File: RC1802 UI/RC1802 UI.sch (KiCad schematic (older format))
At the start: 44 parts, among them J1 Mount, J2 Mount, J3 Mount, J4 Mount, J6 CONN_02X20, SW1 CLEAR, SW10 IN5, SW11 IN6, SW12 IN7, SW2 IN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

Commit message: Fixed issue with in button, seems I should have read missing datasheet!
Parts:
- removed SW2: IN, switches:SPDT_PUSH, symbol SW_Push_SPDT
- added SW2: IN, switches:SPDT_PUSH, symbol NO/NC_Switch
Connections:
- net GND: now also SW2.3 (NC)
- net VCC: now also SW2.2 (NO)
- net at U1.3, U1.8: now also SW2.1 (C)
- no-connect marks 18 -> 17
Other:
- moved on the sheet: AFF1, AFF2, D1, D2, D3, D4, D5, D6, D7, J6, R1, R2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

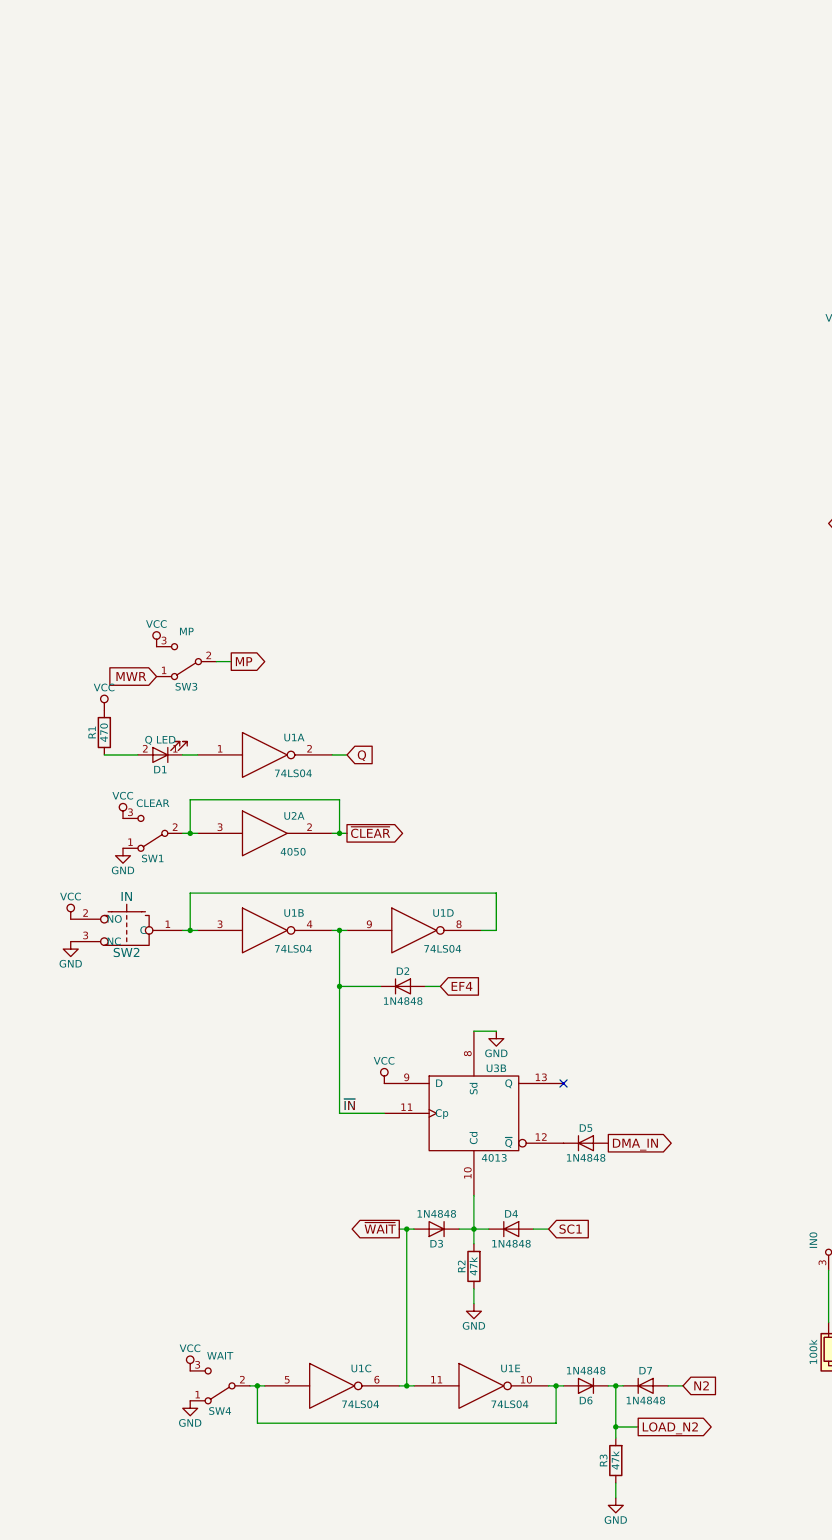
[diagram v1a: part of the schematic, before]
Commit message: Q signal inverter wrong way around!
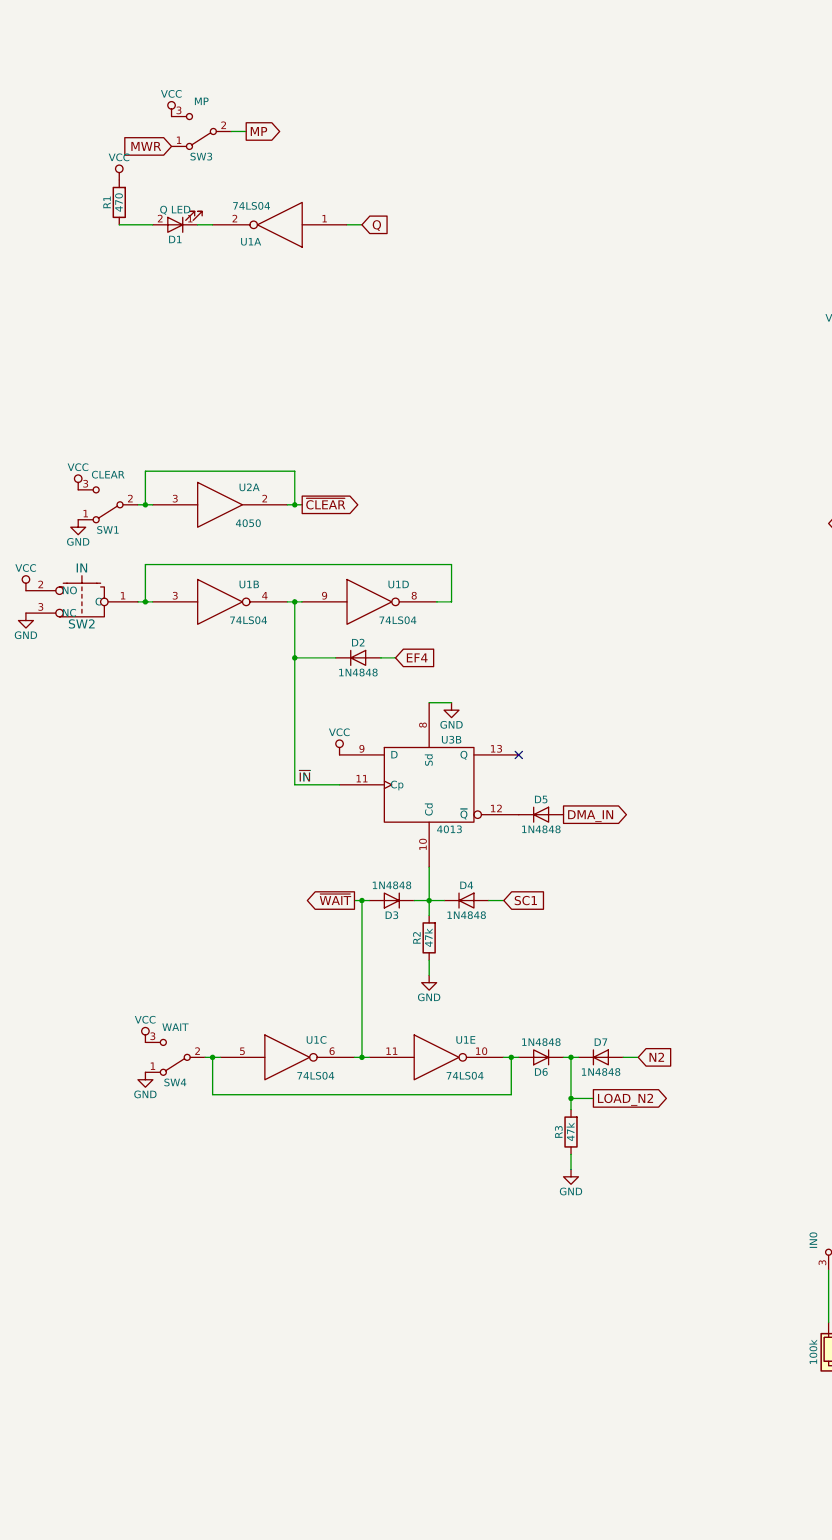
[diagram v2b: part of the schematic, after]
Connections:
- net Q: now also U1.1; no longer U1.2
- net at D1.1 (K): now also U1.2; no longer U1.1
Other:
- moved on the sheet: D1, D2, D3, D4, D5, D6, D7, R1, R2, R3, SW1, SW2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

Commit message: Bus connected in wrong order to hex drivers
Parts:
- AFF1: value MSB -> MSD
- AFF2: value LSB -> LSD
- U6: value 74LS245 -> 74LS244; symbol 74HC245 -> 74LS244
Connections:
- net BUS0: now also U7.5 (A); no longer U7.10 (D)
- net BUS1: now also U6.16 (O1a), U7.6 (B); no longer U6.17 (B1), U7.9 (C)
- net BUS2: now also U6.14 (O2a), U7.9 (C); no longer U6.16 (B2), U7.6 (B)
- net BUS3: now also U6.12 (O3a), U7.10 (D); no longer U6.15 (B3), U7.5 (A)
- net BUS4: now also U5.5 (A), U6.9 (O0b); no longer U5.10 (D), U6.14 (B4)
- net BUS5: now also U5.6 (B), U6.7 (O1b); no longer U5.9 (C), U6.13 (B5)
- net BUS6: now also U5.9 (C), U6.5 (O2b); no longer U5.6 (B), U6.12 (B6)
- net BUS7: now also U5.10 (D), U6.3 (O3b); no longer U5.5 (A), U6.11 (B7)
- net GND: no longer U2.7
- net LOAD_N2: now also U4.10; no longer U4.9
- net READ: now also U2.6, U6.1 (OEa); no longer U4.6
- net TPB: now also U4.11; no longer U4.10
- net VCC: no longer U6.1 (A->B)
- net at SW6.2 (B): now also U6.4 (I1a); no longer U6.3 (A1)
- net at SW7.2 (B): now also U6.6 (I2a); no longer U6.4 (A2)
- net at SW8.2 (B): now also U6.8 (I3a); no longer U6.5 (A3)
- net at SW9.2 (B): now also U6.11 (I0b); no longer U6.6 (A4)
- net at SW10.2 (B): now also U6.13 (I1b); no longer U6.7 (A5)
- net at SW11.2 (B): now also U6.15 (I2b); no longer U6.8 (A6)
- net at SW12.2 (B): now also U6.17 (I3b); no longer U6.9 (A7)
- net at U4.12: now also U4.9; no longer U4.11
- new net: U2.7, U4.6
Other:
- moved on the sheet: RN1, SW10, SW11, SW12, SW5, SW6, SW7, SW8, SW9, U2B, U2C, U4A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

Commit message: Removed resistor array as not in original schematic
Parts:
- removed RN1: 100k, Resistors_THT:R_Array_SIP9, symbol R_Network08
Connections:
- net VCC: now also SW10.3 (C), SW11.3 (C), SW12.3 (C), SW5.3 (C), SW6.3 (C), SW7.3 (C), SW8.3 (C), SW9.3 (C)
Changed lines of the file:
@@
 L VCC #PWR028
 U 1 1 595A4155
-P 6775 7700
-F 0 "#PWR028" H 6775 7550 50  0001 C CNN
-F 1 "VCC" H 6775 7850 50  0000 C CNN
-F 2 "" H 6775 7700 50  0001 C CNN
-F 3 "" H 6775 7700 50  0001 C CNN
-	1    6775 7700
-	0    1    1    0
+P 5775 7150
+F 0 "#PWR028" H 5775 7000 50  0001 C CNN
+F 1 "VCC" H 5775 7300 50  0000 C CNN
+F 2 "" H 5775 7150 50  0001 C CNN
+F 3 "" H 5775 7150 50  0001 C CNN
+	1    5775 7150
+	1    0    0    -1
 $EndComp
 $Comp
@@
 	14375 900  14375 950
 Connection ~ 14375 900
-$Comp
-L R_Network08 RN1
-U 1 1 594D0AD4
-P 6375 7500
-F 0 "RN1" V 5875 7500 50  0000 C CNN
-F 1 "100k" V 6775 7500 50  0000 C CNN
-F 2 "Resistors_THT:R_Array_SIP9" V 6850 7500 50  0001 C CNN
-F 3 "" H 6375 7500 50  0001 C CNN
-	1    6375 7500
-	-1   0    0    1
-$EndComp
 Wire Wire Line
 	6075 6950 6075 7300
@@
 	9675 7275 9675 6950
 Wire Wire Line
-	6775 7300 10275 7300
+	5775 7300 10275 7300
 Wire Wire Line
 	10275 7300 10275 6950
@@
 Wire Wire Line
 	6950 9475 7200 9475
+Connection ~ 6675 7300
+Connection ~ 6575 7300
+Connection ~ 6475 7300
+Connection ~ 6375 7300
+Connection ~ 6275 7300
+Connection ~ 6175 7300
+Connection ~ 6075 7300
+Wire Wire Line
+	5775 7150 5775 7300
 $EndSCHEMATC

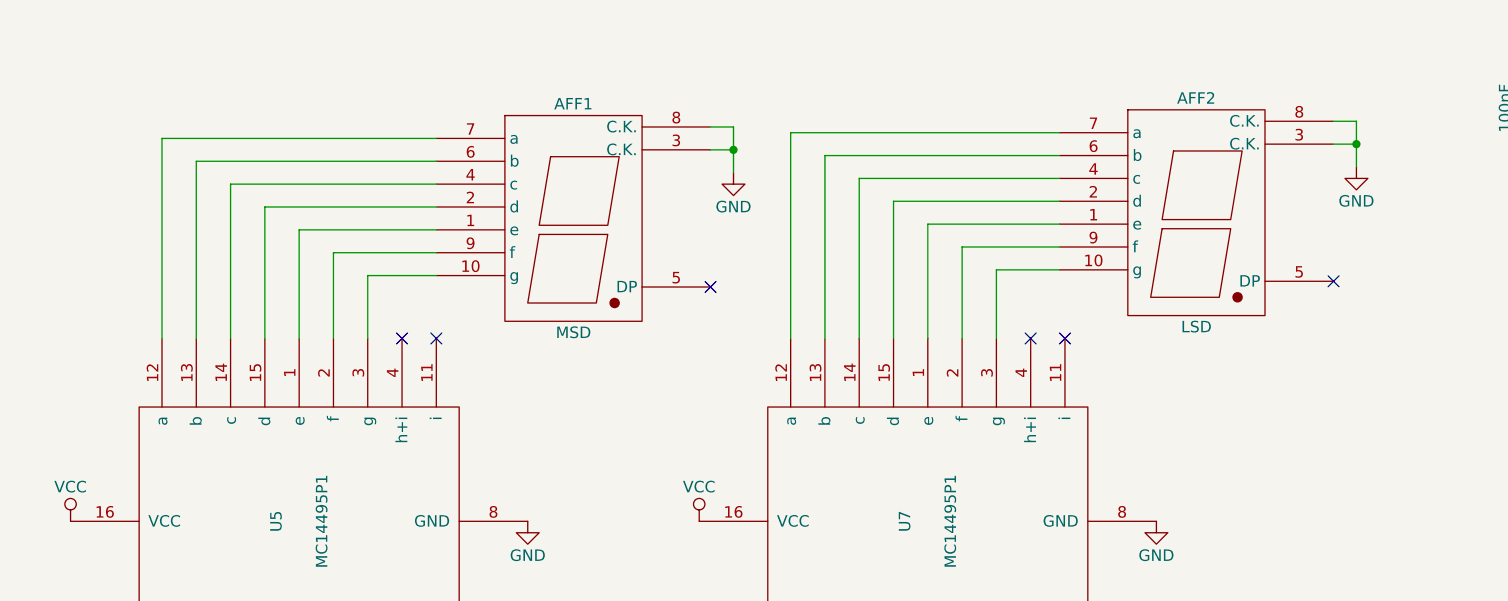
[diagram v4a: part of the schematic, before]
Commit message: Use LED digit DP as STROBE/READ indicator
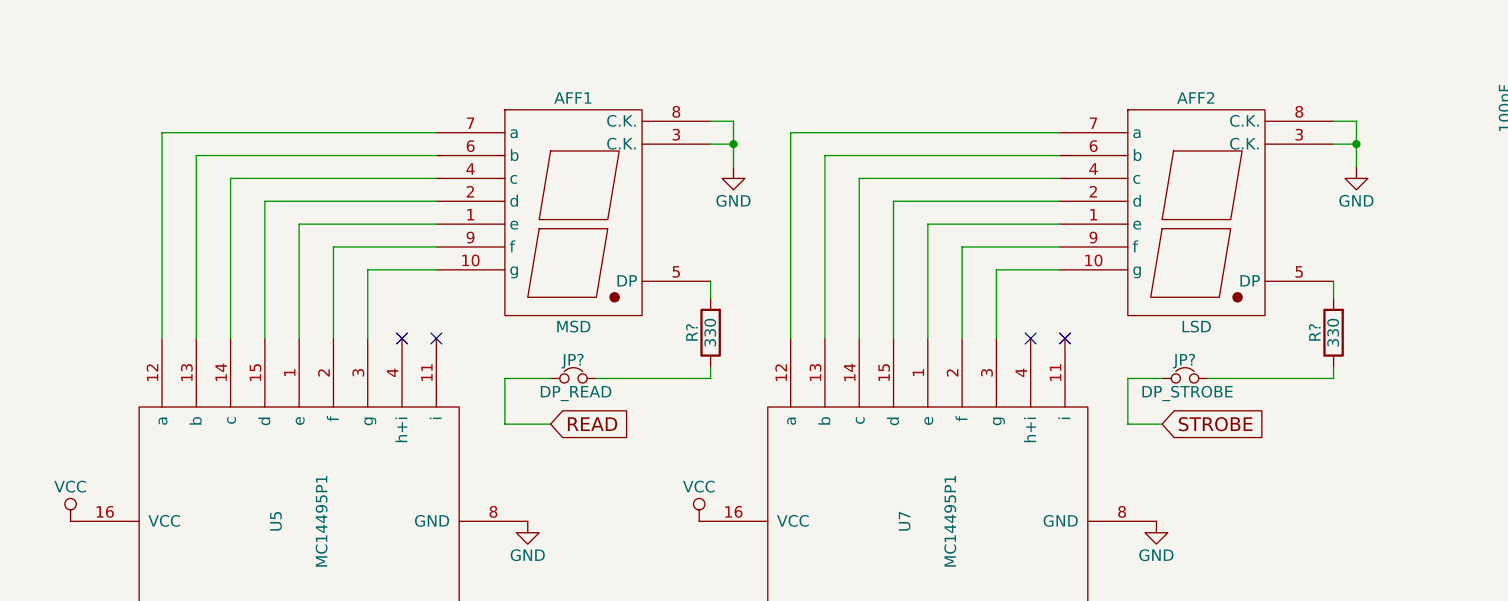
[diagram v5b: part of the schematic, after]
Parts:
- added JP?: DP_READ, symbol Jumper_NC_Small
- added JP?: DP_STROBE, symbol Jumper_NC_Small
- added R? (x2): 330, Resistors_THT:R_Axial_DIN0207_L6.3mm_D2.5mm_P10.16mm_Horizontal, symbol R
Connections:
- net READ: now also JP?.1
- net STROBE: now also JP?.1
- net at AFF1.5 (DP): now also R?.2
- net at AFF2.5 (DP): now also R?.2
- new net: JP?.2, R?.1 (x2)
- no-connect marks 17 -> 15
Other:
- moved on the sheet: AFF1
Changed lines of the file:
@@
 L LTS-6980HR AFF1
 U 1 1 594DB067
-P 8550 1575
-F 0 "AFF1" H 8550 2125 50  0000 C CNN
-F 1 "MSD" H 8550 1125 50  0000 C CNN
-F 2 "Displays_7-Segment:7SegmentLED_LTS6760_LTS6780" H 8550 1575 50  0001 C CNN
-F 3 "" H 8550 1575 50  0001 C CNN
-	1    8550 1575
+P 8550 1550
+F 0 "AFF1" H 8550 2100 50  0000 C CNN
+F 1 "MSD" H 8550 1100 50  0000 C CNN
+F 2 "Displays_7-Segment:7SegmentLED_LTS6760_LTS6780" H 8550 1550 50  0001 C CNN
+F 3 "" H 8550 1550 50  0001 C CNN
+	1    8550 1550
 	1    0    0    -1
 $EndComp
@@
 L GND #PWR026
 U 1 1 594DDA60
-P 9250 1325
-F 0 "#PWR026" H 9250 1075 50  0001 C CNN
-F 1 "GND" H 9250 1175 50  0000 C CNN
-F 2 "" H 9250 1325 50  0001 C CNN
-F 3 "" H 9250 1325 50  0001 C CNN
-	1    9250 1325
+P 9250 1300
+F 0 "#PWR026" H 9250 1050 50  0001 C CNN
+F 1 "GND" H 9250 1150 50  0000 C CNN
+F 2 "" H 9250 1300 50  0001 C CNN
+F 3 "" H 9250 1300 50  0001 C CNN
+	1    9250 1300
 	1    0    0    -1
 $EndComp
@@
 	1    0    0    -1
 $EndComp
-NoConn ~ 9150 1825
-NoConn ~ 11875 1800
 NoConn ~ 10550 2050
 NoConn ~ 10700 2050
@@
 	6850 3650 6850 3975
 Wire Wire Line
-	7950 1775 7650 1775
-Wire Wire Line
-	7650 1775 7650 2050
-Wire Wire Line
-	7950 1675 7500 1675
-Wire Wire Line
-	7500 1675 7500 2050
-Wire Wire Line
-	7950 1575 7350 1575
-Wire Wire Line
-	7350 1575 7350 2050
-Wire Wire Line
-	7200 2050 7200 1475
-Wire Wire Line
-	7200 1475 7950 1475
-Wire Wire Line
-	7950 1375 7050 1375
-Wire Wire Line
-	7050 1375 7050 2050
-Wire Wire Line
-	6900 2050 6900 1275
-Wire Wire Line
-	6900 1275 7950 1275
-Wire Wire Line
-	6750 2050 6750 1175
-Wire Wire Line
-	6750 1175 7950 1175
-Wire Wire Line
-	9150 1225 9250 1225
-Wire Wire Line
-	9250 1125 9250 1325
-Wire Wire Line
-	9250 1125 9150 1125
-Connection ~ 9250 1225
+	7950 1750 7650 1750
+Wire Wire Line
+	7650 1750 7650 2050
+Wire Wire Line
+	7950 1650 7500 1650
+Wire Wire Line
+	7500 1650 7500 2050
+Wire Wire Line
+	7950 1550 7350 1550
+Wire Wire Line
+	7350 1550 7350 2050
+Wire Wire Line
+	7200 1450 7200 2050
+Wire Wire Line
+	7200 1450 7950 1450
+Wire Wire Line
+	7950 1350 7050 1350
+Wire Wire Line
+	7050 1350 7050 2050
+Wire Wire Line
+	6900 1250 6900 2050
+Wire Wire Line
+	6900 1250 7950 1250
+Wire Wire Line
+	6750 1150 6750 2050
+Wire Wire Line
+	6750 1150 7950 1150
+Wire Wire Line
+	9150 1200 9250 1200
+Wire Wire Line
+	9250 1100 9250 1300
+Wire Wire Line
+	9250 1100 9150 1100
+Connection ~ 9250 1200
 Wire Wire Line
 	11875 1200 11975 1200
@@
 Wire Wire Line
 	5775 7150 5775 7300
+$Comp
+L Jumper_NC_Small JP?
+U 1 1 5B990FBF
+P 8550 2225
+F 0 "JP?" H 8550 2305 50  0000 C CNN
+F 1 "DP_READ" H 8560 2165 50  0000 C CNN
+F 2 "" H 8550 2225 50  0001 C CNN
+F 3 "" H 8550 2225 50  0001 C CNN
+	1    8550 2225
+	1    0    0    -1
+$EndComp
+Wire Wire Line
+	8650 2225 9150 2225
+$Comp
+L Jumper_NC_Small JP?
+U 1 1 5B99266E
+P 11225 2225
+F 0 "JP?" H 11225 2305 50  0000 C CNN
+F 1 "DP_STROBE" H 11235 2165 50  0000 C CNN
+F 2 "" H 11225 2225 50  0001 C CNN
+F 3 "" H 11225 2225 50  0001 C CNN
+	1    11225 2225
+	1    0    0    -1
+$EndComp
+Wire Wire Line
+	11875 2225 11325 2225
+Text GLabel 11125 2425 2    60   Input ~ 0
+STROBE
+Wire Wire Line
+	11125 2425 10975 2425
+Wire Wire Line
+	10975 2425 10975 2225
+Wire Wire Line
+	10975 2225 11125 2225
+Text GLabel 8450 2425 2    60   Input ~ 0
+READ
+Wire Wire Line
+	8450 2425 8250 2425
+Wire Wire Line
+	8250 2425 8250 2225
+Wire Wire Line
+	8250 2225 8450 2225
+$Comp
+L R R?
+U 1 1 5B995582
+P 11875 2025
+F 0 "R?" V 11955 2025 50  0000 C CNN
+F 1 "330" V 11875 2025 50  0000 C CNN
+F 2 "Resistors_THT:R_Axial_DIN0207_L6.3mm_D2.5mm_P10.16mm_Horizontal" V 11805 2025 50  0001 C CNN
+F 3 "" H 11875 2025 50  0001 C CNN
+	1    11875 2025
+	-1   0    0    1
+$EndComp
+Wire Wire Line
+	11875 2175 11875 2225
+Wire Wire Line
+	11875 1875 11875 1800
+$Comp
+L R R?
+U 1 1 5B995F7C
+P 9150 2025
+F 0 "R?" V 9230 2025 50  0000 C CNN
+F 1 "330" V 9150 2025 50  0000 C CNN
+F 2 "Resistors_THT:R_Axial_DIN0207_L6.3mm_D2.5mm_P10.16mm_Horizontal" V 9080 2025 50  0001 C CNN
+F 3 "" H 9150 2025 50  0001 C CNN
+	1    9150 2025
+	-1   0    0    1
+$EndComp
+Wire Wire Line
+	9150 1800 9150 1875
+Wire Wire Line
+	9150 2225 9150 2175
 $EndSCHEMATC

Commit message: Added ~Q to UI connector
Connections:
- net GND: now also U1.1; no longer J6.26 (P26)
- net Q: no longer U1.1
- net at U1.2: no longer D1.1 (K)
- new net ~Q: D1.1 (K), J6.26 (P26)
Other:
- moved on the sheet: D1, J6, R1, U1A

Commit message: Regenerate netlist
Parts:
- JP1, JP2: renamed from JP?; footprint (none) -> Pin_Headers:Pin_Header_Straight_1x02_Pitch2.54mm
- gave numbers to parts that had none: 2
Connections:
- net Q: no longer names the net of J6.25 (P25)
- no-connect marks 15 -> 16
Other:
- moved on the sheet: AFF1, AFF2, JP1, JP2, R4, R5, U5, U7

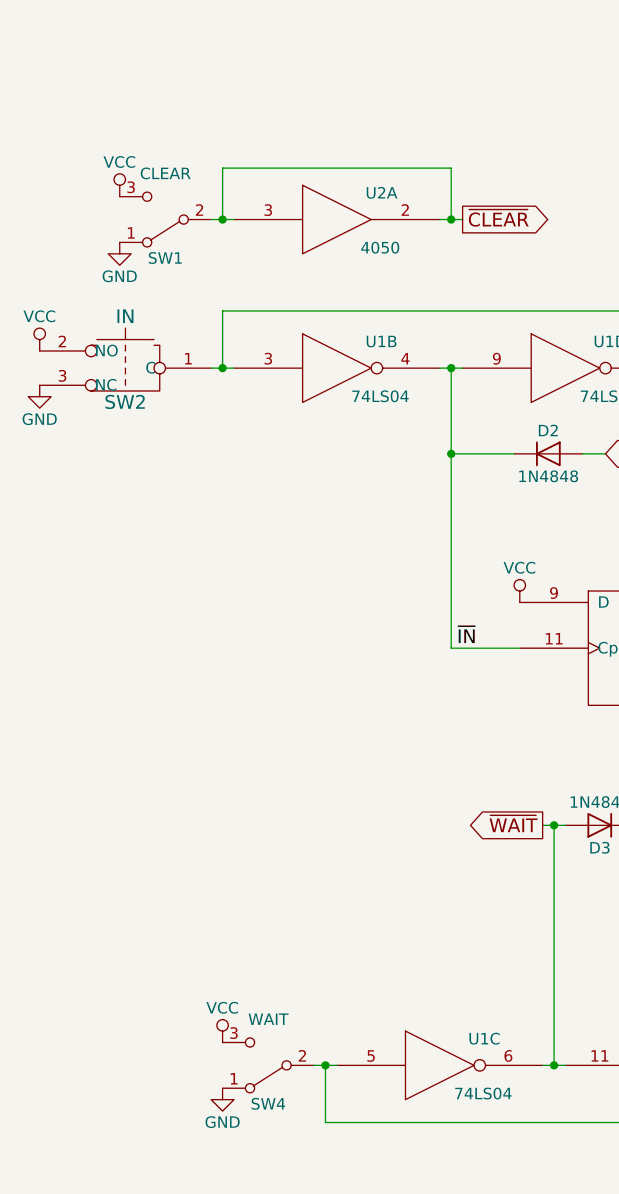
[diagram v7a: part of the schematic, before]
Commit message: Use proper switch names to ease use
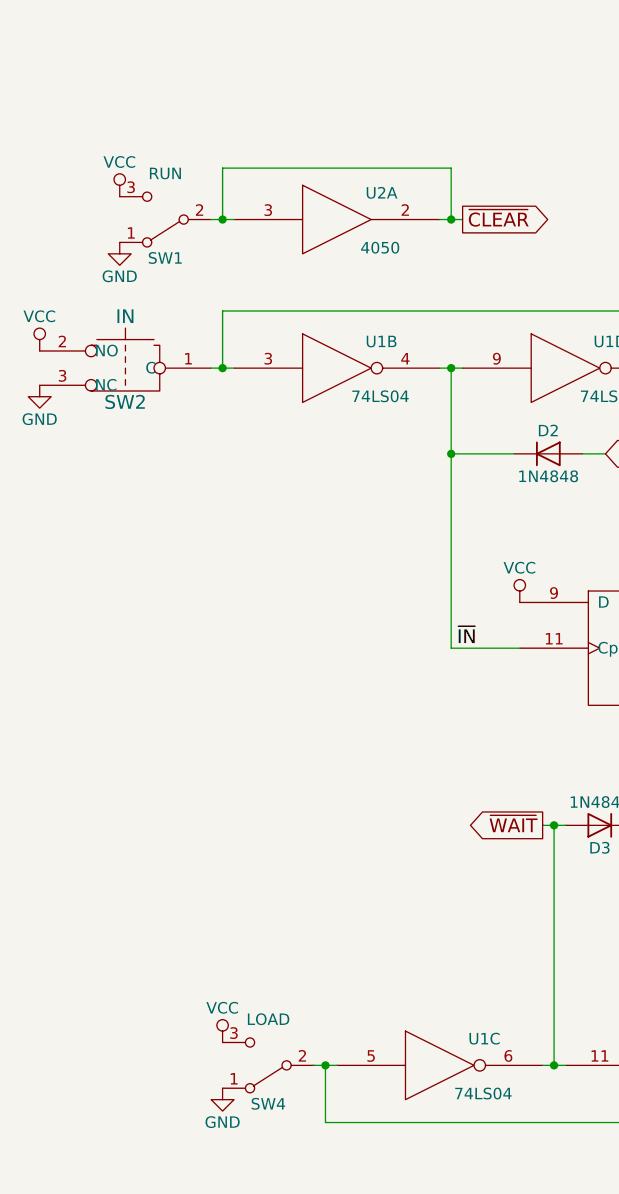
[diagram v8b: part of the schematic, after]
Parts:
- SW1: value CLEAR -> RUN
- SW4: value WAIT -> LOAD
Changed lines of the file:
@@
 P 1475 3950
 F 0 "SW1" H 1475 4120 50  0000 C CNN
-F 1 "CLEAR" H 1475 3750 50  0000 C CNN
+F 1 "RUN" H 1475 3750 50  0000 C CNN
 F 2 "switches:SPDT_SWITCH" H 1475 3950 50  0001 C CNN
 F 3 "" H 1475 3950 50  0001 C CNN
@@
 P 1925 7650
 F 0 "SW4" H 1925 7820 50  0000 C CNN
-F 1 "WAIT" H 1925 7450 50  0000 C CNN
+F 1 "LOAD" H 1925 7450 50  0000 C CNN
 F 2 "switches:SPDT_SWITCH" H 1925 7650 50  0001 C CNN
 F 3 "" H 1925 7650 50  0001 C CNN
